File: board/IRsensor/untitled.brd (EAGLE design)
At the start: 100 x 100 mm, 27 parts

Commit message: Commit
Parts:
- added R4, R5: 1k, generic:SMD1608
- added RXLED, TXLED: (no value), led:SML0603
- moved C1 60.5 mm to (-0.51, -16.6), turned to 180 degrees
- moved C2 57.9 mm to (2.67, -16.6), turned to 0 degrees
- moved C3 49.4 mm to (10.3, -32.1), turned to 270 degrees
- moved C4 46.7 mm to (13.1, -32.1)
- moved C5 44.2 mm to (15.9, -32.1)
- moved JP1 34.5 mm to (0.00, -14.0)
- moved R1 30.7 mm to (-8.89, -19.1)
- moved R2 29.0 mm to (-6.35, -19.1)
- moved R3 16.8 mm to (7.62, -16.9), turned to 90 degrees
- moved Q1 1.80 mm to (1.27, -20.3)
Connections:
- removed net N$1: U$1.18
- removed net N$10: U$1.19
- removed net N$14: IR1.3, IR2.3, IR3.3, IR4.3
- removed net N$18: IR2.1
- removed net N$21: U$1.27
- removed net N$22: U$1.26
- removed net N$23: U$1.25
- removed net N$26: IR1.2, IR2.2, IR3.2, IR4.2
- removed net N$28: IR1.1
- removed net N$29: U$1.28
- removed net N$30: IR4.1
- removed net N$31: IR3.1
- removed net N$33: IR8.1
- removed net N$64: IR7.1
- removed net N$79: IR15.1
- new net IR1: IR1.1, U$1.19
- new net IR14: IR14.1, U$1.32
- new net IR15: IR15.1, U$1.31
- new net IR16: IR16.1, U$1.30
- new net IR2: IR2.1, U$1.25
- new net IR3: IR3.1, U$1.26
- new net IR4: IR4.1, U$1.27
- new net IR5: IR5.1, U$1.28
- new net IR6: IR6.1, U$1.29
- new net IR7: IR7.1, U$1.1
- new net IR8: IR8.1, U$1.41
- new net N$11: R4.2, U$1.22
- new net N$15: R4.1, TXLED.A
- net +5V: now also IR1.3, IR2.3, IR3.3, IR4.3, JP1.8; no longer JP1.6
- net D+: now also JP1.2; no longer JP1.3
- net D-: now also JP1.1; no longer JP1.2
- net GNDA: now also IR1.2, IR2.2, IR3.2, IR4.2, JP1.7, RXLED.C, TXLED.C; no longer JP1.8
- net N$16: now also R5.1, RXLED.A; no longer U$1.41
- net N$2: now also JP1.4; no longer JP1.7
- net N$3: now also JP1.3; no longer JP1.5
- net N$44: now also R5.2
- net RESET: now also JP1.5; no longer JP1.4
- net UVCC: now also JP1.6; no longer JP1.1
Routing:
- net GNDA: track 0.00 -> 415.1 mm, vias 0 -> 6
- net +5V: track 0.00 -> 359.5 mm, vias 0 -> 5
- net IR1: track 0.00 -> 122.6 mm, vias 0 -> 2
- net IR2: track 0.00 -> 107.8 mm, vias 0 -> 2
- net IR16: track 0.00 -> 101.2 mm
- net IR3: track 0.00 -> 93.9 mm, vias 0 -> 2
- net IR15: track 0.00 -> 86.9 mm
- net IR4: track 0.00 -> 78.6 mm, vias 0 -> 2
- net IR14: track 0.00 -> 72.7 mm
- net IR5: track 0.00 -> 65.2 mm, vias 0 -> 2
- net IR6: track 0.00 -> 49.0 mm, vias 0 -> 2
- net UVCC: track 0.00 -> 39.0 mm, vias 0 -> 2
- net IR7: track 0.00 -> 22.2 mm, vias 0 -> 2
- net N$8: track 0.00 -> 20.8 mm, vias 0 -> 2
- net RESET: track 0.00 -> 18.8 mm, vias 0 -> 2
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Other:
- outline, holes or cut-outs redrawn
- board text added: "Designed by hirame"

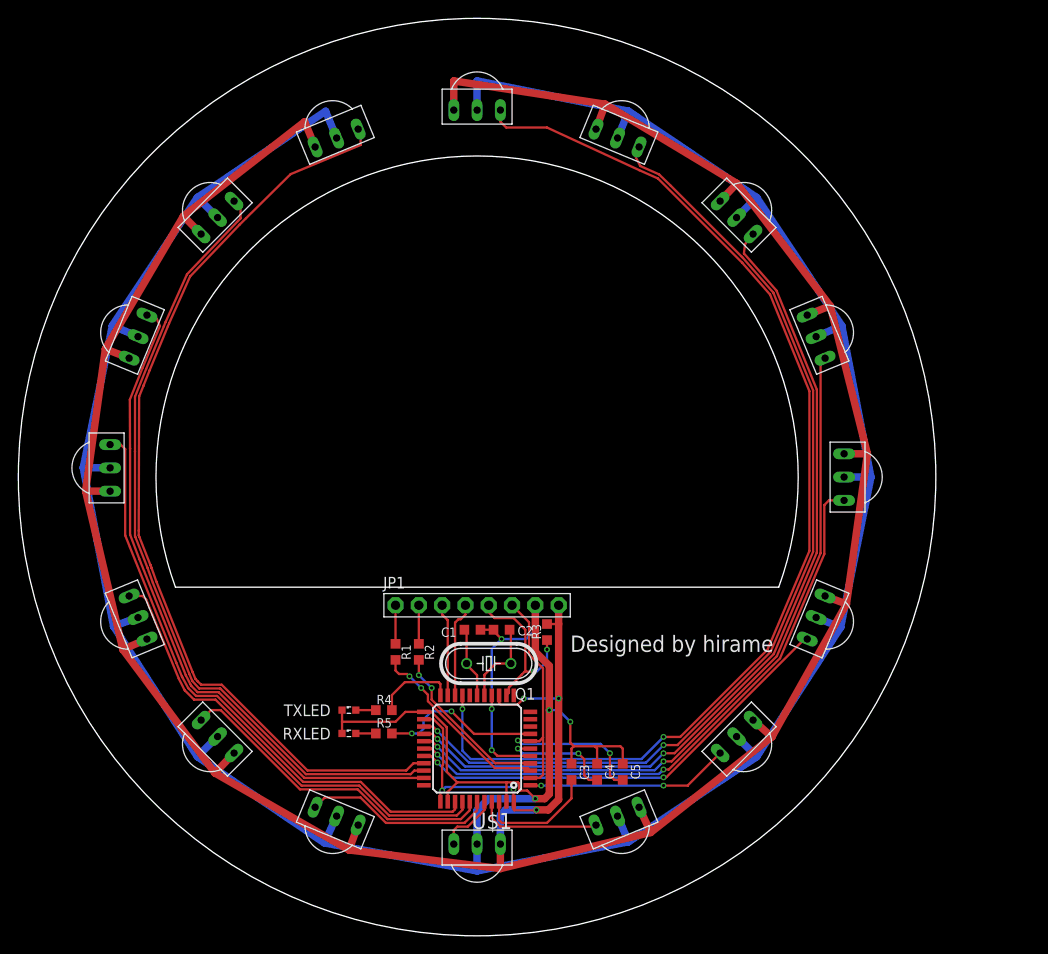
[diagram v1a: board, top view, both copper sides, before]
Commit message: renewal ir sensor board
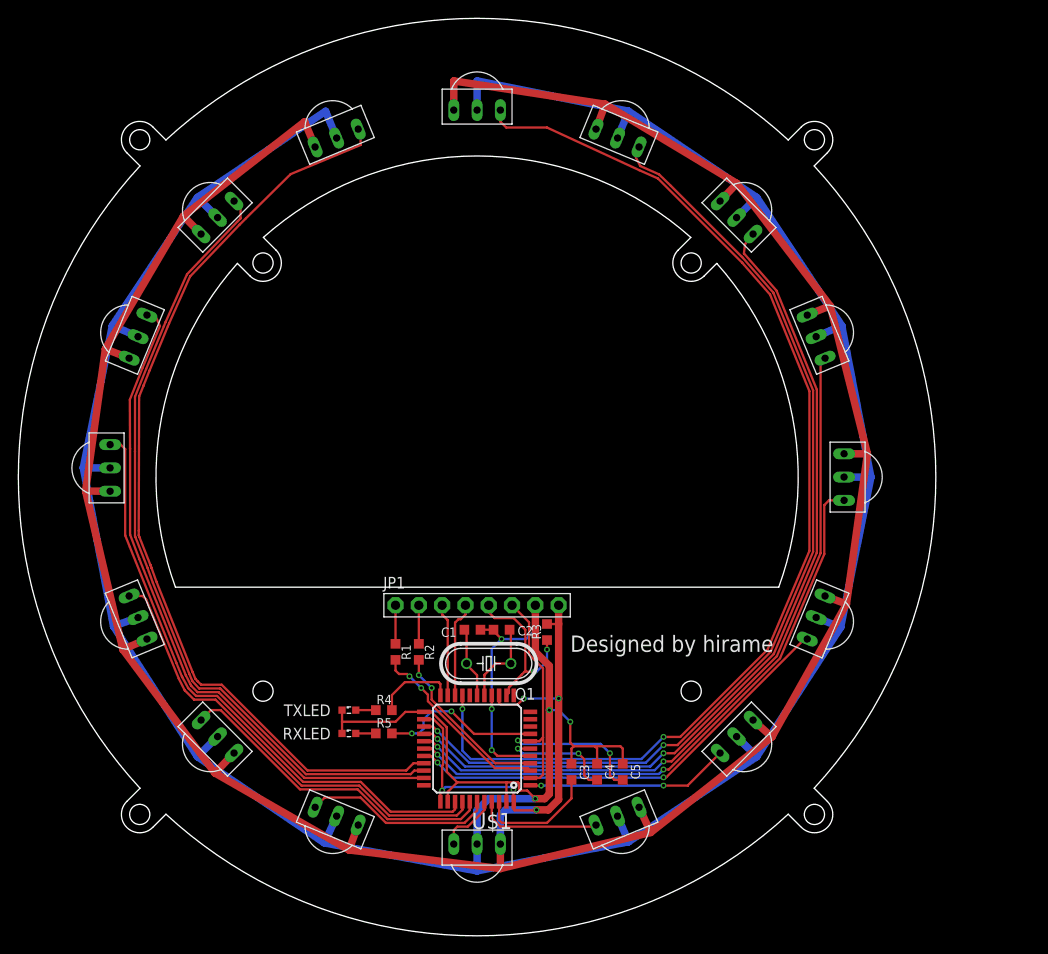
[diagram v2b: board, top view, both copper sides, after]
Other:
- outline, holes or cut-outs redrawn
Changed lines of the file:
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@@
 <?xml version="1.0" encoding="utf-8"?>
 <!DOCTYPE eagle SYSTEM "eagle.dtd">
-<eagle version="9.6.2">
+<eagle version="9.6.1">
 <drawing>
 <settings>
-<setting alwaysvectorfont="yes"/>
+<setting alwaysvectorfont="no"/>
 <setting verticaltext="up"/>
 </settings>
@@
 <plain>
 <text x="10.16" y="-19.05" size="1.778" layer="25">Designed by hirame</text>
-<circle x="0" y="0" radius="50" width="0.001" layer="20"/>
 <wire x1="32.878559375" y1="-12" x2="-32.878559375" y2="-12" width="0.001" layer="20"/>
-<wire x1="32.878559375" y1="-12" x2="-32.878559375" y2="-12" width="0.001" layer="20" curve="220.102091"/>
+<circle x="23.33451875" y="23.33451875" radius="1.1" width="0.001" layer="20"/>
+<wire x1="23.29408125" y1="26.122509375" x2="21.920309375" y2="24.748740625" width="0.001" layer="20"/>
+<wire x1="24.748740625" y1="21.920309375" x2="26.122509375" y2="23.29408125" width="0.001" layer="20"/>
+<wire x1="21.920309375" y1="24.748740625" x2="24.748740625" y2="21.920309375" width="0.001" layer="20" curve="180"/>
+<circle x="-23.33451875" y="23.33451875" radius="1.1" width="0.001" layer="20"/>
+<wire x1="-26.122509375" y1="23.29408125" x2="-24.748740625" y2="21.920309375" width="0.001" layer="20"/>
+<wire x1="-21.920309375" y1="24.748740625" x2="-23.29408125" y2="26.122509375" width="0.001" layer="20"/>
+<wire x1="-24.748740625" y1="21.920309375" x2="-21.920309375" y2="24.748740625" width="0.001" layer="20" curve="180"/>
+<circle x="23.33451875" y="-23.33451875" radius="1.1" width="0.001" layer="20"/>
+<circle x="-23.33451875" y="-23.33451875" radius="1.1" width="0.001" layer="20"/>
+<wire x1="32.878559375" y1="-12" x2="26.122509375" y2="23.29408125" width="0.001" layer="20" curve="61.775215"/>
+<wire x1="23.29408125" y1="26.122509375" x2="-23.29408125" y2="26.122509375" width="0.001" layer="20" curve="83.448339"/>
+<wire x1="-26.122509375" y1="23.29408125" x2="-32.878559375" y2="-12" width="0.001" layer="20" curve="61.775215"/>
+<wire x1="36.741259375" y1="-33.91283125" x2="36.741259375" y2="33.91283125" width="0.001" layer="20" curve="85.415113"/>
+<wire x1="33.91283125" y1="36.741259375" x2="-33.91283125" y2="36.741259375" width="0.001" layer="20" curve="85.415113"/>
+<wire x1="-36.741259375" y1="33.91283125" x2="-36.741259375" y2="-33.91283125" width="0.001" layer="20" curve="85.415113"/>
+<wire x1="-33.91283125" y1="-36.741259375" x2="33.91283125" y2="-36.741259375" width="0.001" layer="20" curve="85.415113"/>
+<wire x1="35.355340625" y1="38.18376875" x2="33.91283125" y2="36.741259375" width="0.001" layer="20"/>
+<wire x1="38.18376875" y1="35.355340625" x2="36.741259375" y2="33.91283125" width="0.001" layer="20"/>
+<circle x="36.76955" y="36.76955" radius="1.1" width="0.001" layer="20"/>
+<wire x1="38.18376875" y1="35.355340625" x2="35.355340625" y2="38.18376875" width="0.001" layer="20" curve="179.99962"/>
+<wire x1="38.18376875" y1="-35.355340625" x2="36.741259375" y2="-33.91283125" width="0.001" layer="20"/>
+<wire x1="35.355340625" y1="-38.18376875" x2="33.91283125" y2="-36.741259375" width="0.001" layer="20"/>
+<circle x="36.76955" y="-36.76955" radius="1.1" width="0.001" layer="20"/>
+<wire x1="35.355340625" y1="-38.18376875" x2="38.18376875" y2="-35.355340625" width="0.001" layer="20" curve="179.99962"/>
+<wire x1="-35.355340625" y1="-38.18376875" x2="-33.91283125" y2="-36.741259375" width="0.001" layer="20"/>
+<wire x1="-38.18376875" y1="-35.355340625" x2="-36.741259375" y2="-33.91283125" width="0.001" layer="20"/>
+<circle x="-36.76955" y="-36.76955" radius="1.1" width="0.001" layer="20"/>
+<wire x1="-38.18376875" y1="-35.355340625" x2="-35.355340625" y2="-38.18376875" width="0.001" layer="20" curve="179.99962"/>
+<wire x1="-38.18376875" y1="35.355340625" x2="-36.741259375" y2="33.91283125" width="0.001" layer="20"/>
+<wire x1="-35.355340625" y1="38.18376875" x2="-33.91283125" y2="36.741259375" width="0.001" layer="20"/>
+<circle x="-36.76955" y="36.76955" radius="1.1" width="0.001" layer="20"/>
+<wire x1="-35.355340625" y1="38.18376875" x2="-38.18376875" y2="35.355340625" width="0.001" layer="20" curve="179.99962"/>
 </plain>
 <attributes>
